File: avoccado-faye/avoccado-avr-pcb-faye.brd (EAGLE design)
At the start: 25 x 24.5 mm, 56 parts, among them Q1 16MHz, Q2 FET, U2 MCP73831

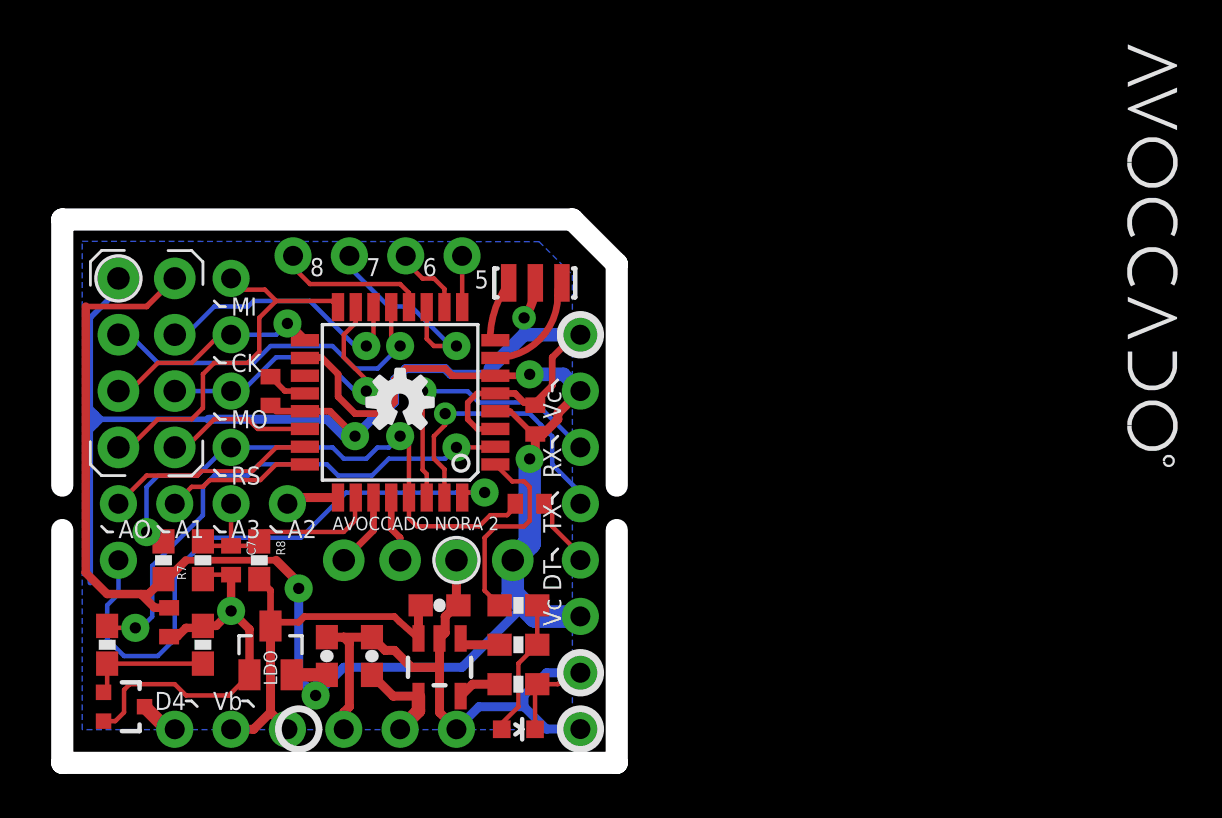
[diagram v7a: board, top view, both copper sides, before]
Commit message: all signals routed to spec
TODO: snap to grid, silkscreen
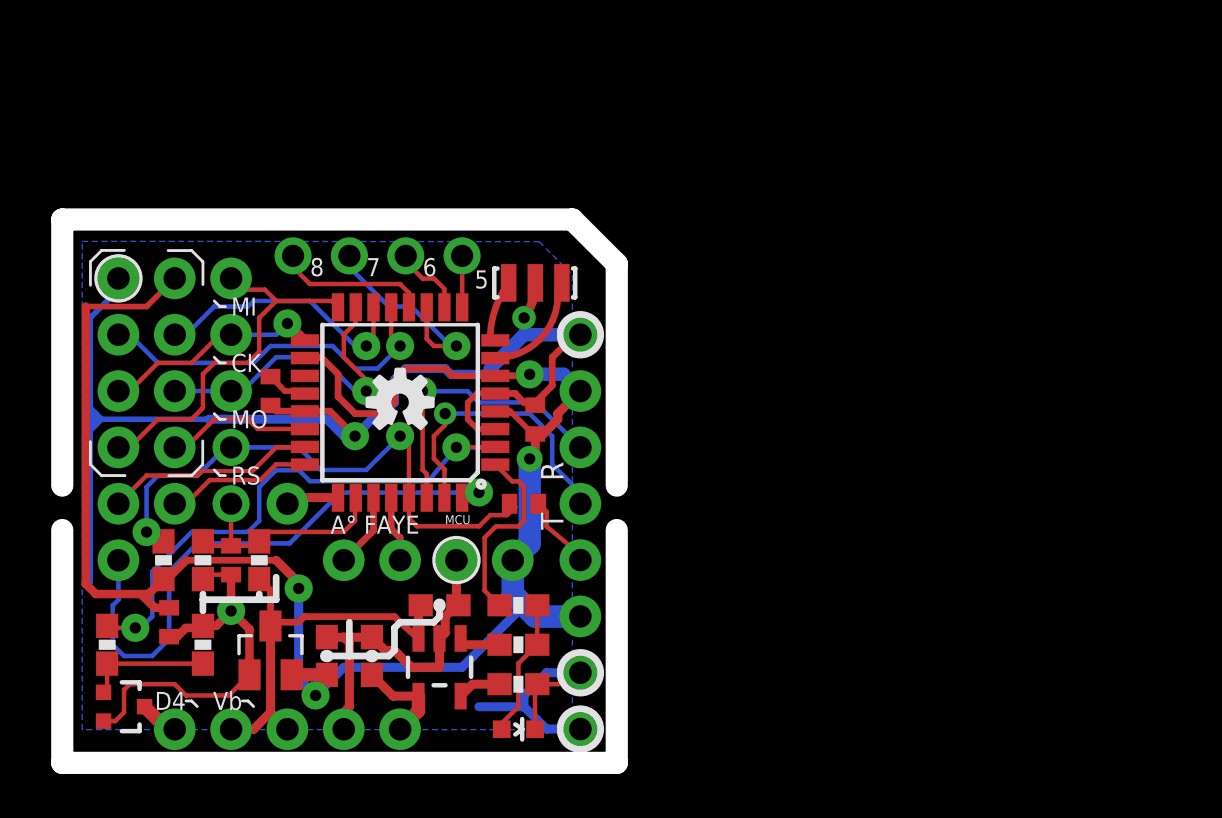
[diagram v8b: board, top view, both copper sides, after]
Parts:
- removed AVR: ATMEGA328P, SparkFun-DigitalIC:TQFP32-08
- removed JP7: M01NOSILK-KIT, SparkFun-Connectors:1X01NS-KIT
- added MCU: ATMEGA328P_TQFP, SparkFun-DigitalIC:TQFP32-08
- JP1, JP10, JP11, JP12, JP13, JP14, JP17, JP18, JP19, JP20, JP21, JP23, JP24, JP25, JP26, JP3, JP6, JP8, JP9, TP2: value M01NOSILK-KIT -> M01PTH; device SparkFun-Connectors:1X01NS-KIT -> SparkFun-Connectors:1X01
- R3: value Rchg -> RP
- moved C2 0.25 mm to (20.3, 11.2)
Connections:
- net 3.3V: now also MCU.18, MCU.4, MCU.6; no longer AVR.18, AVR.4, AVR.6
- net A0: now also MCU.23; no longer AVR.23
- net A1: now also MCU.24; no longer AVR.24
- net A2: now also MCU.25; no longer AVR.25
- net A3: now also MCU.26; no longer AVR.26
- net A4: now also MCU.27; no longer AVR.27
- net A5: now also MCU.28; no longer AVR.28
- net A6: now also MCU.19; no longer AVR.19
- net A7-NRF-IRQ: now also MCU.22; no longer AVR.22
- net AREF: now also MCU.20; no longer AVR.20
- net D10: now also MCU.14; no longer AVR.14
- net D2: now also MCU.32; no longer AVR.32
- net D3: now also MCU.1; no longer AVR.1
- net D4: now also MCU.2; no longer AVR.2
- net D5: now also MCU.9; no longer AVR.9
- net D6: now also MCU.10; no longer AVR.10
- net D7: now also MCU.11; no longer AVR.11
- net D8: now also MCU.12; no longer AVR.12
- net D9: now also MCU.13; no longer AVR.13
- net GND: now also MCU.21, MCU.3, MCU.5; no longer AVR.21, AVR.3, AVR.5, JP7.1
- net MISO: now also MCU.16; no longer AVR.16
- net MOSI: now also MCU.15; no longer AVR.15
- net N$1: now also MCU.8; no longer AVR.8
- net N$2: now also MCU.7; no longer AVR.7
- net RESET: now also MCU.29; no longer AVR.29
- net RXI: now also MCU.30; no longer AVR.30
- net SCK: now also MCU.17; no longer AVR.17
- net TXO: now also MCU.31; no longer AVR.31
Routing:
- net GND: track 108.6 -> 104.1 mm
- net D3: track 10.1 -> 9.15 mm
- net D2: track 27.0 -> 26.3 mm
- net RESET: track 25.1 -> 25.7 mm
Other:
- board text added: "A° FAYE"
- board text added: "R"
- board text added: "T"
- board text removed: "AVOCCADO NORA 2"
